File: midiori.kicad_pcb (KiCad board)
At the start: 2 copper layers, 141 x 150 mm, 45 parts, among them J1 x68000_expansion, J2 Conn_ARM_JTAG_SWD_10, J4 Mini-DIN-5, U1 74LCX07, U10 ICE40HX1K-VQ100, U11 TLV73333PDBV, U2 AT25SF081-SSHD-X, U3 TLV73312PDBV, U4 SN74LVC8T245DWR, U5 SN74LVC8T245DWR, U6 SN74LVC8T245DWR, U7 SN74LVC8T245DWR, U8 SN74LVC8T245DWR, U9 SN74LVC8T245DWR, X1 16MHz

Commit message: convert pcb version
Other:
- net class Default removed

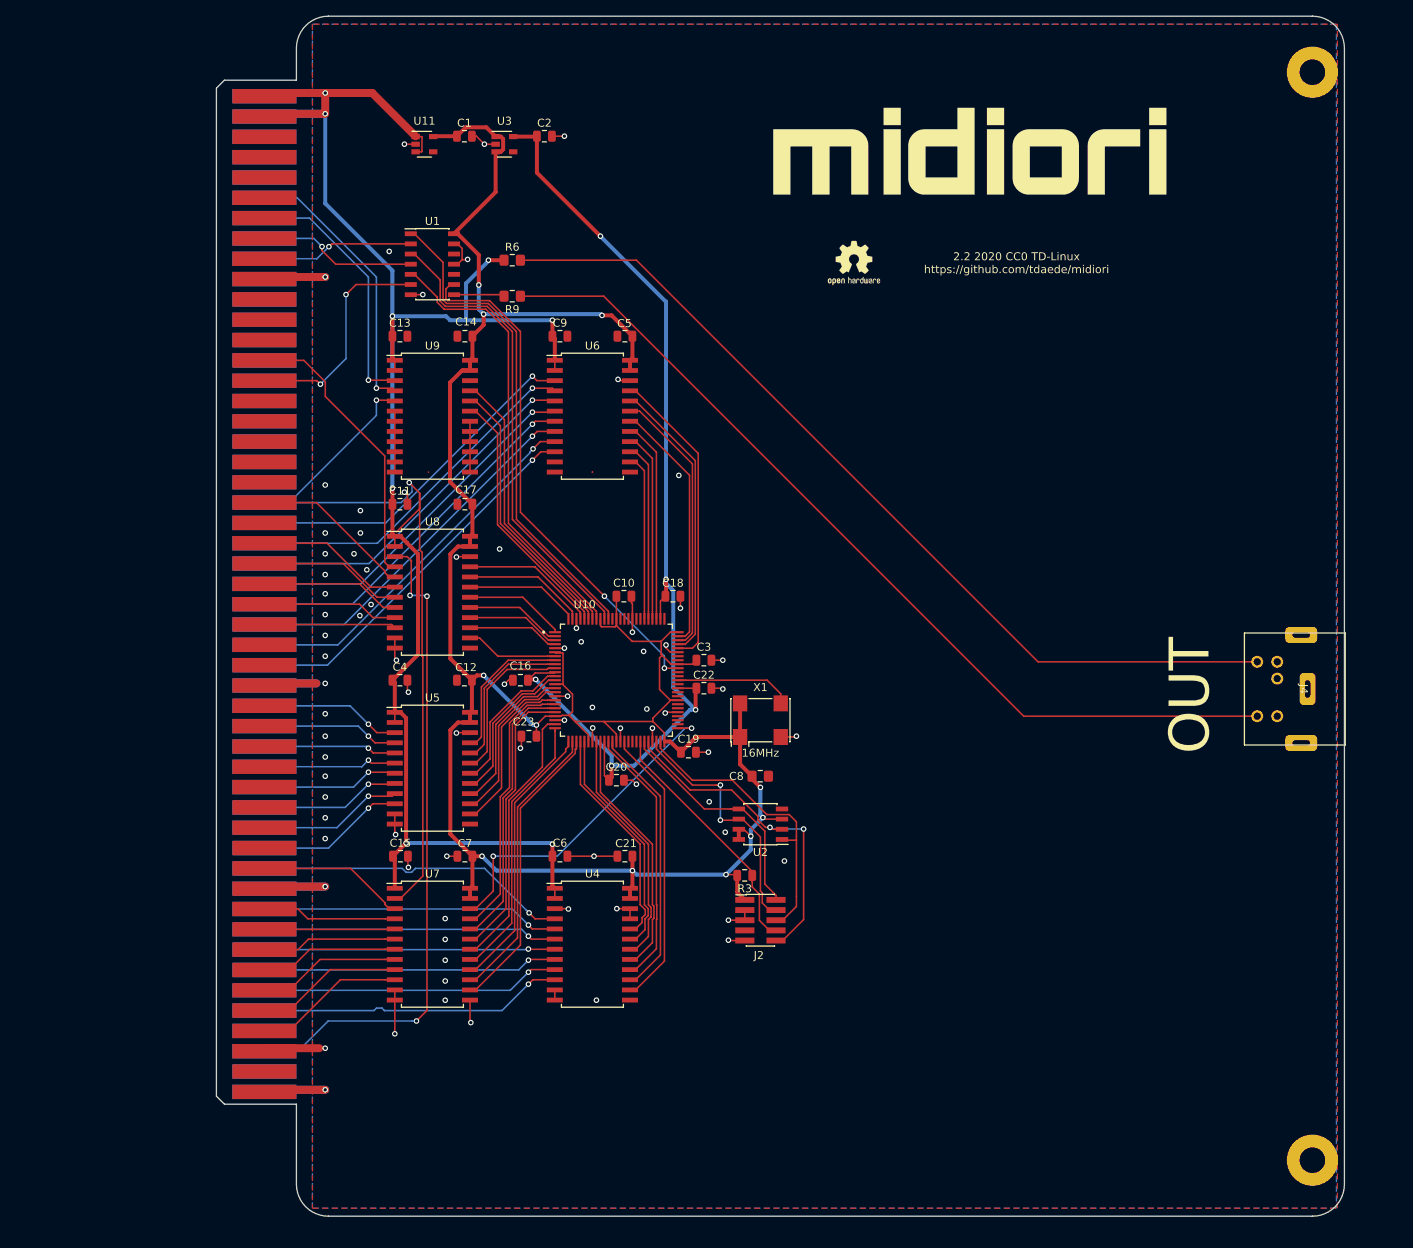
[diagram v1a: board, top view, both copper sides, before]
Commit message: switch to single psu translator
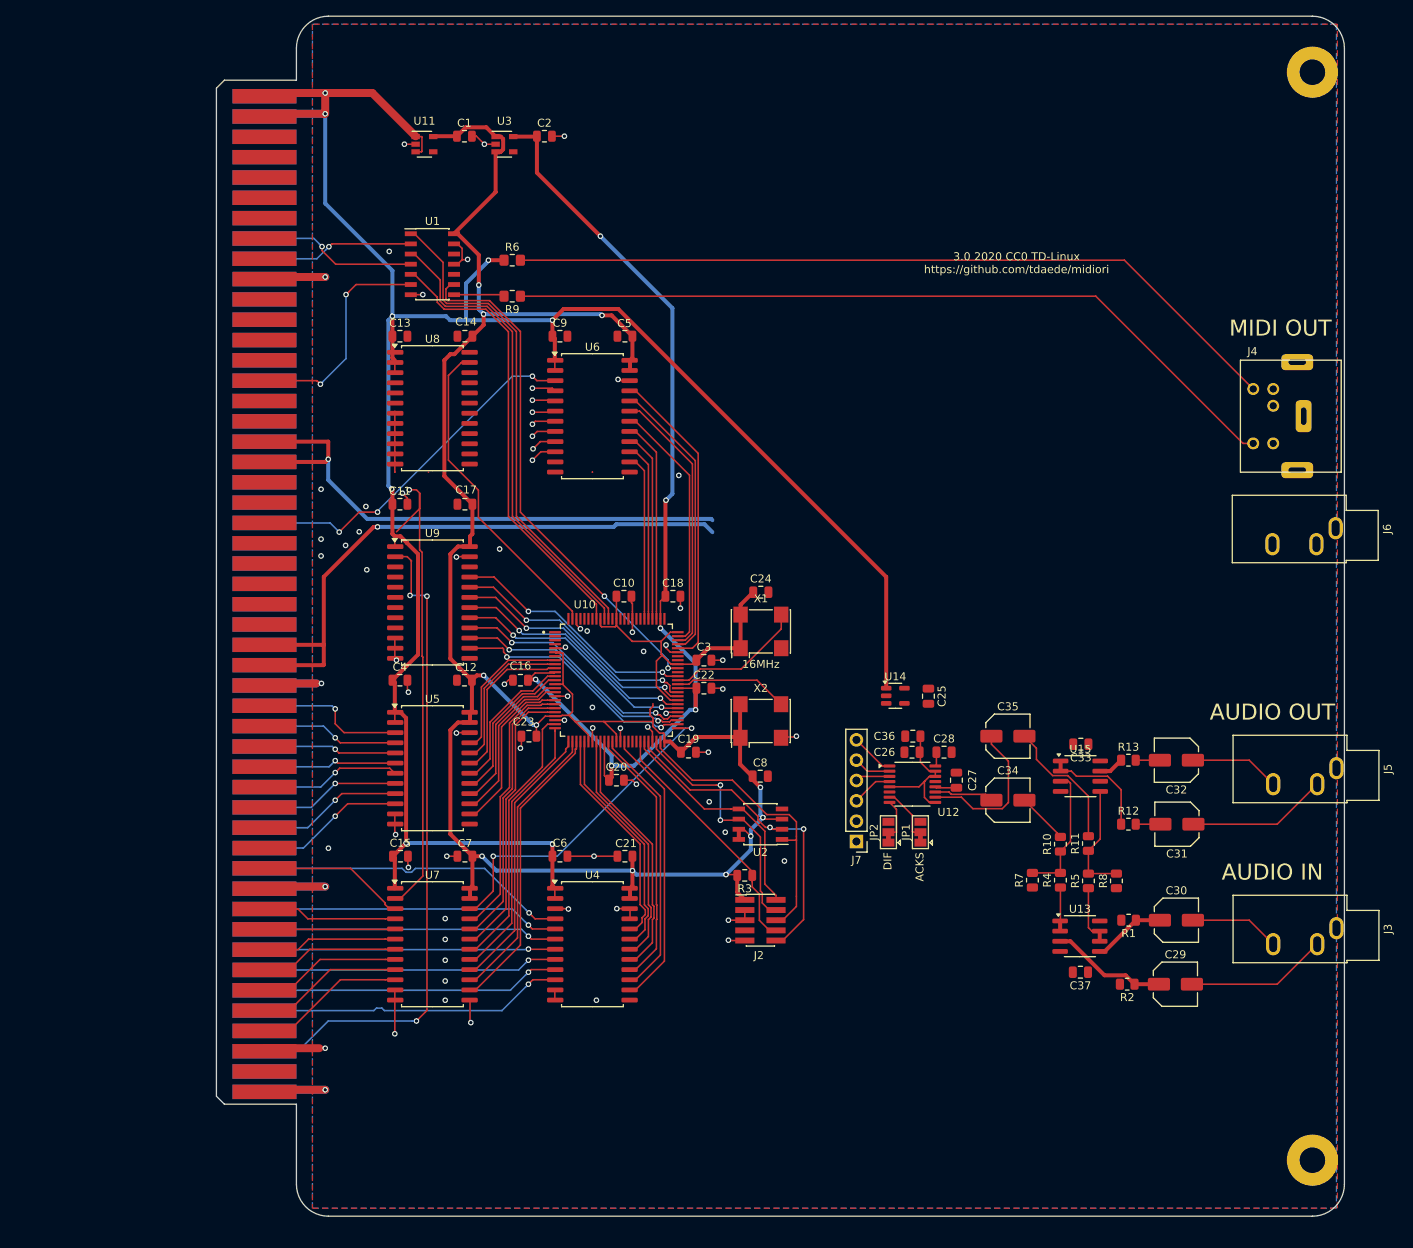
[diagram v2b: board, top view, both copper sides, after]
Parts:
- removed REF**: OSHW-Logo2_7.3x6mm_SilkScreen, Symbol:OSHW-Logo2_7.3x6mm_SilkScreen
- removed svg2mod: G***, x68k:midiori_logo
- added C24: 0.1uF, Capacitor_SMD:C_0805_2012Metric, F.Cu at (112.0, 111.0)
- added C25: 4.7uF, Capacitor_SMD:C_0805_2012Metric, F.Cu at (133.0, 124.0)
- added C26: 0.1uF, Capacitor_SMD:C_0805_2012Metric, F.Cu at (130.9, 131.0)
- added C27: 2.2uF, Capacitor_SMD:C_0805_2012Metric, F.Cu at (136.5, 134.5)
- added C28: 1uF, Capacitor_SMD:C_0805_2012Metric, F.Cu at (134.9, 131.0)
- added C29: 10uF, Capacitor_SMD:C_Elec_5x5.8, F.Cu at (163.9, 160.0)
- added C30: 10uF, Capacitor_SMD:C_Elec_5x5.8, F.Cu at (164.0, 152.0)
- added C31: 10uF, Capacitor_SMD:C_Elec_5x5.8, F.Cu at (164.1, 140.0)
- added C32: 10uF, Capacitor_SMD:C_Elec_5x5.8, F.Cu at (164.0, 132.0)
- added C33: 0.1uF, Capacitor_SMD:C_0805_2012Metric, F.Cu at (152.1, 130.0)
- added C34: 10uF, Capacitor_SMD:C_Elec_5x5.8, F.Cu at (142.9, 137.0)
- added C35: 10uF, Capacitor_SMD:C_Elec_5x5.8, F.Cu at (142.9, 129.0)
- added C36: 4.7uF, Capacitor_SMD:C_0805_2012Metric, F.Cu at (131.1, 129.0)
- added C37: 0.1uF, Capacitor_SMD:C_0805_2012Metric, F.Cu at (152.0, 158.5)
- added J3: AudioJack3, Connector_Audio:Jack_3.5mm_CUI_SJ1-3533NG_Horizontal, F.Cu at (184.0, 153.0)
- added J5: AudioJack3, Connector_Audio:Jack_3.5mm_CUI_SJ1-3533NG_Horizontal, F.Cu at (184.0, 133.0)
- added J6: AudioJack3, Connector_Audio:Jack_3.5mm_CUI_SJ1-3533NG_Horizontal, F.Cu at (183.9, 103.0)
- added J7: Conn_01x06, Connector_PinHeader_2.54mm:PinHeader_1x06_P2.54mm_Vertical, F.Cu at (124.0, 142.2)
- added JP1: ACKS, Jumper:SolderJumper-3_P1.3mm_Bridged12_Pad1.0x1.5mm, F.Cu at (132.0, 141.0)
- added JP2: DIF, Jumper:SolderJumper-3_P1.3mm_Bridged12_Pad1.0x1.5mm, F.Cu at (128.0, 141.0)
- added R1: 10k, Resistor_SMD:R_0805_2012Metric, F.Cu at (158.0, 152.0)
- added R10: 10k, Resistor_SMD:R_0805_2012Metric, F.Cu at (149.5, 142.5)
- added R11: 10k, Resistor_SMD:R_0805_2012Metric, F.Cu at (153.0, 142.4)
- added R12: 1k, Resistor_SMD:R_0805_2012Metric, F.Cu at (158.0, 140.0)
- added R13: 1k, Resistor_SMD:R_0805_2012Metric, F.Cu at (158.0, 132.0)
- added R2: 10k, Resistor_SMD:R_0805_2012Metric, F.Cu at (157.8, 160.0)
- added R4: 10k, Resistor_SMD:R_0805_2012Metric, F.Cu at (149.5, 147.0)
- added R5: 10k, Resistor_SMD:R_0805_2012Metric, F.Cu at (153.0, 147.1)
- added R7: 10k, Resistor_SMD:R_0805_2012Metric, F.Cu at (146.0, 147.0)
- added R8: 10k, Resistor_SMD:R_0805_2012Metric, F.Cu at (156.5, 147.1)
- added U12: AK4432, Package_SO:TSSOP-16_4.4x5mm_P0.65mm, F.Cu at (131.0, 135.0)
- added U13: TL074, Package_SO:SOIC-8_3.9x4.9mm_P1.27mm, F.Cu at (151.9, 154.0)
- added U14: AP2205K-3.3, Package_TO_SOT_SMD:SOT-23-5, F.Cu at (128.9, 124.0)
- added U15: TL072, Package_SO:SOIC-8_3.9x4.9mm_P1.27mm, F.Cu at (152.0, 134.0)
- added X2: 24.576MHz, Oscillator:Oscillator_SMD_SeikoEpson_SG8002CA-4Pin_7.0x5.0mm, F.Cu at (112.0, 127.1)
- C8: footprint Capacitor_SMD:C_0805_2012Metric_Pad1.15x1.40mm_HandSolder -> Capacitor_SMD:C_0805_2012Metric
- J1: value x68000_expansion -> midiori-rescue_x68000_expansion-x68k-midiori-rescue
- U11: value TLV73333PDBV -> AP2205K-3.3
- U3: value TLV73312PDBV -> AP2127K-1.2
- moved J4 34.1 mm to (179.9, 89.0)
- moved U9 23.3 mm to (71.0, 112.3)
- moved U8 23.0 mm to (71.0, 88.0)
- moved X1 11.1 mm to (112.1, 115.9)
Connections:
- net Net-(J4-Pad4) renamed /source
- net Net-(J4-Pad5) renamed /sink
- net Net-(U10-Pad63) renamed /16mhz
- J1 pad A13: Net-(J1-PadA13) -> /DB8
- J1 pad A14: Net-(J1-PadA14) -> /DB9
- J1 pad A15: Net-(J1-PadA15) -> /DB10
- J1 pad A16: Net-(J1-PadA16) -> /DB11
- J1 pad A17: Net-(J1-PadA17) -> /DB12
- J1 pad A18: Net-(J1-PadA18) -> /DB13
- J1 pad A19: Net-(J1-PadA19) -> /DB14
- J1 pad A2: Net-(J1-PadA2) -> unconnected-(J1-PadA2)
- J1 pad A20: Net-(J1-PadA20) -> /DB15
- J1 pad A22: Net-(J1-PadA22) -> +12V
- J1 pad A23: Net-(J1-PadA23) -> +12V
- J1 pad A24: /C -> unconnected-(J1-FC0-PadA24)
- J1 pad A25: /B -> unconnected-(J1-FC1-PadA25)
- J1 pad A26: /A -> unconnected-(J1-FC2-PadA26)
- J1 pad A29: Net-(J1-PadA29) -> unconnected-(J1-PadA29)
- J1 pad A31: Net-(J1-PadA31) -> unconnected-(J1-PadA31)
- J1 pad A32: Net-(J1-PadA32) -> -12V
- J1 pad A33: Net-(J1-PadA33) -> -12V
- J1 pad A34: Net-(J1-PadA34) -> unconnected-(J1-PadA34)
- J1 pad A35: Net-(J1-PadA35) -> unconnected-(J1-PadA35)
- J1 pad A38: Net-(J1-PadA38) -> unconnected-(J1-PadA38)
- J1 pad A39: Net-(J1-PadA39) -> unconnected-(J1-PadA39)
- J1 pad A40: Net-(J1-PadA40) -> unconnected-(J1-PadA40)
- J1 pad A42: Net-(J1-PadA42) -> unconnected-(J1-PadA42)
- J1 pad A43: Net-(J1-PadA43) -> unconnected-(J1-PadA43)
- J1 pad A44: Net-(J1-PadA44) -> unconnected-(J1-PadA44)
- J1 pad A45: Net-(J1-PadA45) -> unconnected-(J1-PadA45)
- J1 pad A46: Net-(J1-PadA46) -> unconnected-(J1-PadA46)
- J1 pad A47: Net-(J1-PadA47) -> unconnected-(J1-PadA47)
- J1 pad A48: Net-(J1-PadA48) -> unconnected-(J1-PadA48)
- J1 pad B2: Net-(J1-PadB2) -> unconnected-(J1-PadB2)
- J1 pad B31: Net-(J1-PadB31) -> unconnected-(J1-PadB31)
- J1 pad B32: Net-(J1-PadB32) -> unconnected-(J1-PadB32)
- J1 pad B33: Net-(J1-PadB33) -> unconnected-(J1-PadB33)
- J1 pad B34: Net-(J1-PadB34) -> unconnected-(J1-PadB34)
- J1 pad B35: Net-(J1-PadB35) -> unconnected-(J1-PadB35)
- J1 pad B36: Net-(J1-PadB36) -> unconnected-(J1-PadB36)
- J1 pad B37: Net-(J1-PadB37) -> unconnected-(J1-PadB37)
- J1 pad B38: Net-(J1-PadB38) -> unconnected-(J1-PadB38)
- J1 pad B39: Net-(J1-PadB39) -> unconnected-(J1-PadB39)
- J1 pad B4: Net-(J1-PadB4) -> unconnected-(J1-PadB4)
- J1 pad B40: Net-(J1-PadB40) -> unconnected-(J1-PadB40)
- J1 pad B46: Net-(J1-PadB46) -> unconnected-(J1-PadB46)
- J1 pad B47: Net-(J1-PadB47) -> unconnected-(J1-PadB47)
- J1 pad B48: Net-(J1-PadB48) -> unconnected-(J1-PadB48)
- J2 pad 7: Net-(J2-Pad7) -> unconnected-(J2-KEY-Pad7)
- J4 pad 1: Net-(J4-Pad1) -> unconnected-(J4-Pad1)
- J4 pad 3: Net-(J4-Pad3) -> unconnected-(J4-Pad3)
- U1 pad 10: Net-(U1-Pad10) -> unconnected-(U1-Pad10)
- U1 pad 12: Net-(U1-Pad12) -> unconnected-(U1-Pad12)
- U10 pad 3: /a -> unconnected-(U10-IOL_2A-Pad3)
- U10 pad 4: /b -> unconnected-(U10-IOL_2B-Pad4)
- U10 pad 41: Net-(U10-Pad41) -> unconnected-(U10-IOB_42_CBSEL0-Pad41)
- U10 pad 42: Net-(U10-Pad42) -> unconnected-(U10-IOB_43_CBSEL1-Pad42)
- U10 pad 43: Net-(U10-Pad43) -> unconnected-(U10-CDONE-Pad43)
- U10 pad 52: Net-(U10-Pad52) -> /db8
- U10 pad 53: Net-(U10-Pad53) -> /db9
- U10 pad 54: Net-(U10-Pad54) -> /db10
- U10 pad 56: Net-(U10-Pad56) -> /db11
- U10 pad 57: Net-(U10-Pad57) -> /db12
- U10 pad 59: Net-(U10-Pad59) -> /db13
- U10 pad 60: Net-(U10-Pad60) -> /db14
- U10 pad 62: Net-(U10-Pad62) -> /24.576mhz
- U10 pad 64: Net-(U10-Pad64) -> /db15
- U10 pad 65: Net-(U10-Pad65) -> unconnected-(U10-IOR_64-Pad65)
- U10 pad 68: Net-(U10-Pad68) -> unconnected-(U10-IOR_67-Pad68)
- U10 pad 69: Net-(U10-Pad69) -> unconnected-(U10-IOR_68-Pad69)
- U10 pad 7: /c -> unconnected-(U10-IOL_3A-Pad7)
- U10 pad 76: Net-(U10-Pad76) -> unconnected-(U10-VPP_FAST-Pad76)
- U10 pad 82: Net-(U10-Pad82) -> unconnected-(U10-IOT_78-Pad82)
- U10 pad 83: Net-(U10-Pad83) -> unconnected-(U10-IOT_79-Pad83)
- U10 pad 85: Net-(U10-Pad85) -> /smute
- U10 pad 86: Net-(U10-Pad86) -> /sdti
- U10 pad 87: Net-(U10-Pad87) -> /lrck
- U10 pad 89: Net-(U10-Pad89) -> /bick
- U11 pad 4: Net-(U11-Pad4) -> unconnected-(U11-NC-Pad4)
- U3 pad 1: +3V3 -> +5V
- U3 pad 3: +3V3 -> +5V
- U3 pad 4: Net-(U3-Pad4) -> unconnected-(U3-NC-Pad4)
- U8 pad 10: /C -> /IDDIR
- U8 pad 14: /c -> /iddir
- U8 pad 15: /b -> /iack4
- U8 pad 16: /a -> /iack2
- U8 pad 8: /A -> /IACK2
- U8 pad 9: /B -> /IACK4
- U9 pad 10: GND -> /DB8
- U9 pad 14: GND -> /db8
- U9 pad 15: GND -> /db9
- U9 pad 16: GND -> /db10
- U9 pad 17: GND -> /db11
- U9 pad 18: GND -> /db12
- U9 pad 19: /iddir -> /db13
- U9 pad 2: +5V -> /IDDIR
- U9 pad 20: /iack4 -> /db14
- U9 pad 21: /iack2 -> /db15
- U9 pad 22: GND -> /xltr_oe
- U9 pad 3: /IACK2 -> /DB15
- U9 pad 4: /IACK4 -> /DB14
- U9 pad 5: /IDDIR -> /DB13
- U9 pad 6: GND -> /DB12
- U9 pad 7: GND -> /DB11
- U9 pad 8: GND -> /DB10
- U9 pad 9: GND -> /DB9
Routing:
- net +12V: track 0.00 -> 77.6 mm, vias 0 -> 1
- net -12V: track 0.00 -> 71.0 mm, vias 0 -> 2
- net +5V: track 227.3 -> 297.8 mm
- net /AB16: track 47.3 -> 3.24 mm
- net /AB17: track 46.9 -> 3.09 mm
- net /IDDIR: track 103.6 -> 60.1 mm, vias 2 -> 1
- net /AB18: track 49.4 -> 6.15 mm
- net /AB19: track 45.8 -> 2.95 mm
- net /AB20: track 45.2 -> 2.86 mm
- net /AB21: track 44.8 -> 2.84 mm
- net /AB22: track 44.5 -> 2.93 mm
- net /EXRESET: track 35.9 -> 0.00 mm
- net /iack2: track 35.3 -> 0.00 mm
- net /IACK4: track 34.4 -> 0.00 mm, vias 1 -> 0
- net /iack4: track 33.8 -> 0.00 mm
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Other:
- board text added: "3.0 2020 CC0 TD-Linux https://github.com/tdaede/midiori"
- board text added: "ACKS"
- board text added: "AUDIO IN"
- board text added: "AUDIO OUT"
- board text added: "DIF"
- board text added: "MIDI OUT"
- board text removed: "2.2 2020 CC0 TD-Linux https://github.com/tdaede/midiori"
- board text removed: "OUT"

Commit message: aaaaaaaaaaa
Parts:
- removed C11, C13, C15, C4, C6, C9: 0.1uF, Capacitor_SMD:C_0805_2012Metric
- added J8: AudioJack3, Connector_Audio:Jack_3.5mm_CUI_SJ1-3533NG_Horizontal, F.Cu at (183.8, 114.9)
- added J9: Mini-DIN-5, x68k:MD-50SM, F.Cu at (179.9, 101.0)
- added JP3: Jumper_3_Bridged12, Jumper:SolderJumper-3_P1.3mm_Bridged12_Pad1.0x1.5mm, F.Cu at (21.1, 57.4)
- added JP4: Jumper_3_Bridged12, Jumper:SolderJumper-3_P1.3mm_Bridged12_Pad1.0x1.5mm, F.Cu at (21.1, 61.2)
- added JP5: Jumper_3_Bridged12, Jumper:SolderJumper-3_P1.3mm_Bridged12_Pad1.0x1.5mm, F.Cu at (21.1, 65.1)
- added R14: 10k, Resistor_SMD:R_0805_2012Metric, F.Cu at (26.1, 57.1)
- added R15: 220, Resistor_SMD:R_0805_2012Metric, F.Cu at (26.1, 60.0)
- added R16: 220, Resistor_SMD:R_0805_2012Metric, F.Cu at (26.1, 63.0)
- added U16: 74LCX07, Package_SO:SOIC-14_3.9x8.7mm_P1.27mm, F.Cu at (90.0, 80.5)
- added U17: PC817, Package_DIP:DIP-4_W7.62mm, F.Cu at (152.2, 110.7)
- added U18: SN74LVC245APW, Package_SO:SOIC-20W_7.5x12.8mm_P1.27mm, F.Cu at (71.0, 64.0)
- R6, R9: footprint Resistor_SMD:R_0805_2012Metric_Pad1.15x1.40mm_HandSolder -> Resistor_SMD:R_0805_2012Metric
- U4, U5, U6, U7, U8, U9: value SN74LVC8T245DWR -> SN74LVC245APW; footprint Package_SO:SOIC-24W_7.5x15.4mm_P1.27mm -> Package_SO:SOIC-20W_7.5x12.8mm_P1.27mm
- moved C2 56.1 mm to (114.0, 102.1), turned to -90 degrees
- moved U3 55.9 mm to (110.1, 102.0)
- moved R9 33.1 mm to (114.0, 77.0)
- moved R6 26.0 mm to (107.0, 69.0)
- moved U6 22.8 mm to (71.0, 100.0)
- moved U1 20.4 mm to (90.0, 62.5)
- moved J6 20.1 mm to (183.8, 82.9)
- moved J4 20.0 mm to (179.9, 69.0)
- moved U8 6.00 mm to (71.0, 82.0)
- moved U9 5.72 mm to (71.0, 118.0)
- moved U11 4.03 mm to (70.5, 51.0)
- moved U5 3.00 mm to (71.0, 136.0)
- moved C1 2.98 mm to (74.5, 51.1), turned to -90 degrees
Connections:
- net Net-(U10-IOR_65) renamed /midi_out
- J1 pad B36: unconnected-(J1-PadB36) -> /EXREQ
- J1 pad B37: unconnected-(J1-PadB37) -> /EXACK
- J1 pad B39: unconnected-(J1-PadB39) -> /EXOWN
- J1 pad B46: unconnected-(J1-PadB46) -> /BR
- J1 pad B47: unconnected-(J1-PadB47) -> /BG
- J1 pad B48: unconnected-(J1-PadB48) -> /BGACK
- U1 pad 10: unconnected-(U1-Pad10) -> /BR
- U1 pad 11: GND -> /br
- U1 pad 12: unconnected-(U1-Pad12) -> /UDS
- U1 pad 13: GND -> /uds_lds_drv
- U1 pad 5: /dtack -> /dtack_drv
- U10 pad 3: unconnected-(U10-IOL_2A-Pad3) -> /bg
- U10 pad 4: unconnected-(U10-IOL_2B-Pad4) -> /midi_in
- U10 pad 41: unconnected-(U10-IOB_42_CBSEL0-Pad41) -> /rw_drv
- U10 pad 42: unconnected-(U10-IOB_43_CBSEL1-Pad42) -> /as_drv
- U10 pad 65: unconnected-(U10-IOR_64-Pad65) -> /bgack
- U10 pad 68: unconnected-(U10-IOR_67-Pad68) -> /br
- U10 pad 69: unconnected-(U10-IOR_68-Pad69) -> /data_dir
- U10 pad 7: unconnected-(U10-IOL_3A-Pad7) -> /uds_lds_drv
- U10 pad 82: unconnected-(U10-IOT_78-Pad82) -> /dtack
- U10 pad 83: unconnected-(U10-IOT_79-Pad83) -> Net-(JP4-C)
- U10 pad 89: /bick -> /10m
- U10 pad 93: /dtack -> /dtack_drv
- U10 pad 97: /10m -> /exown
- U4 pad 1: +5V -> /addr_dir
- U4 pad 10: /AB1 -> GND
- U4 pad 11: GND -> /a1
- U4 pad 12: GND -> /a2
- U4 pad 13: GND -> /a3
- U4 pad 14: /a1 -> /a4
- U4 pad 15: /a2 -> /a5
- U4 pad 16: /a3 -> /a6
- U4 pad 17: /a4 -> /a7
- U4 pad 18: /a5 -> GND
- U4 pad 19: /a6 -> GND
- U4 pad 2: +5V -> GND
- U4 pad 20: /a7 -> +3V3
- U4 pad 3: GND -> /AB7
- U4 pad 4: /AB7 -> /AB6
- U4 pad 5: /AB6 -> /AB5
- U4 pad 6: /AB5 -> /AB4
- U4 pad 7: /AB4 -> /AB3
- U4 pad 8: /AB3 -> /AB2
- U4 pad 9: /AB2 -> /AB1
- U5 pad 1: +5V -> /addr_dir
- U5 pad 10: /AB8 -> GND
- U5 pad 11: GND -> /ab8
- U5 pad 12: GND -> /ab9
- U5 pad 13: GND -> /ab10
- U5 pad 14: /ab8 -> /ab11
- U5 pad 15: /ab9 -> /ab12
- U5 pad 16: /ab10 -> /ab13
- U5 pad 17: /ab11 -> /ab14
- U5 pad 18: /ab12 -> /ab15
- U5 pad 19: /ab13 -> GND
- U5 pad 2: +5V -> /AB15
- U5 pad 20: /ab14 -> +3V3
- U5 pad 3: /AB15 -> /AB14
- U5 pad 4: /AB14 -> /AB13
- U5 pad 5: /AB13 -> /AB12
- U5 pad 6: /AB12 -> /AB11
- U5 pad 7: /AB11 -> /AB10
- U5 pad 8: /AB10 -> /AB9
- U5 pad 9: /AB9 -> /AB8
- U6 pad 1: +5V -> /addr_dir
- U6 pad 10: /AB16 -> GND
- U6 pad 11: GND -> /a16
- U6 pad 12: GND -> /a17
- U6 pad 13: GND -> /a18
- U6 pad 14: /a16 -> /a19
- U6 pad 15: /a17 -> /a20
- U6 pad 16: /a18 -> /a21
- U6 pad 17: /a19 -> /a22
- U6 pad 18: /a20 -> /a23
- U6 pad 19: /a21 -> GND
- U6 pad 2: +5V -> /AB23
- U6 pad 20: /a22 -> +3V3
- U6 pad 3: /AB23 -> /AB22
- U6 pad 4: /AB22 -> /AB21
- U6 pad 5: /AB21 -> /AB20
- U6 pad 6: /AB20 -> /AB19
- U6 pad 7: /AB19 -> /AB18
- U6 pad 8: /AB18 -> /AB17
- U6 pad 9: /AB17 -> /AB16
- U7 pad 1: +5V -> /data_dir
- U7 pad 10: /DB0 -> GND
- U7 pad 11: GND -> /d0
- U7 pad 12: GND -> /d1
- U7 pad 13: GND -> /d2
- U7 pad 14: /d0 -> /d3
- U7 pad 15: /d1 -> /d4
- U7 pad 16: /d2 -> /d5
- U7 pad 17: /d3 -> /d6
- U7 pad 18: /d4 -> /d7
- U7 pad 19: /d5 -> /xltr_oe
- U7 pad 2: /IDDIR -> /DB7
- U7 pad 20: /d6 -> +3V3
- U7 pad 3: /DB7 -> /DB6
- U7 pad 4: /DB6 -> /DB5
- U7 pad 5: /DB5 -> /DB4
- U7 pad 6: /DB4 -> /DB3
- U7 pad 7: /DB3 -> /DB2
- U7 pad 8: /DB2 -> /DB1
- U7 pad 9: /DB1 -> /DB0
- U8 pad 1: +5V -> +3V3
- U8 pad 10: /IDDIR -> GND
- U8 pad 11: GND -> /iddir
- U8 pad 12: GND -> /iack4
- U8 pad 13: GND -> /iack2
- U8 pad 14: /iddir -> /as
- U8 pad 15: /iack4 -> /lds
- U8 pad 16: /iack2 -> /rw
- U8 pad 17: /as -> /exreset
- U8 pad 18: /lds -> /10m
- U8 pad 19: /rw -> GND
- U8 pad 2: +5V -> /10MHz
- U8 pad 20: /exreset -> +3V3
- U8 pad 3: /10MHz -> /EXRESET
- U8 pad 4: /EXRESET -> /RW
- U8 pad 5: /RW -> /LDS
- U8 pad 6: /LDS -> /AS
- U8 pad 7: /AS -> /IACK2
- U8 pad 8: /IACK2 -> /IACK4
- U8 pad 9: /IACK4 -> /IDDIR
- U9 pad 1: +5V -> /data_dir
- U9 pad 10: /DB8 -> GND
- U9 pad 11: GND -> /db8
- U9 pad 12: GND -> /db9
- U9 pad 13: GND -> /db10
- U9 pad 14: /db8 -> /db11
- U9 pad 15: /db9 -> /db12
- U9 pad 16: /db10 -> /db13
- U9 pad 17: /db11 -> /db14
- U9 pad 18: /db12 -> /db15
- U9 pad 19: /db13 -> /xltr_oe
- U9 pad 2: /IDDIR -> /DB15
- U9 pad 20: /db14 -> +3V3
- U9 pad 3: /DB15 -> /DB14
- U9 pad 4: /DB14 -> /DB13
- U9 pad 5: /DB13 -> /DB12
- U9 pad 6: /DB12 -> /DB11
- U9 pad 7: /DB11 -> /DB10
- U9 pad 8: /DB10 -> /DB9
- U9 pad 9: /DB9 -> /DB8
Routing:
- net +3V3: track 323.9 -> 52.8 mm, vias 12 -> 1
- net +5V: track 297.8 -> 52.2 mm, vias 8 -> 2
- net /10MHz: track 83.1 -> 0.00 mm, vias 3 -> 0
- net /source: track 98.3 -> 22.8 mm
- net /sink: track 99.9 -> 28.0 mm
- net +1V2: track 129.2 -> 61.4 mm, vias 6 -> 4
- net +12V: track 77.6 -> 17.4 mm, vias 1 -> 0
- net /IDDIR: track 60.1 -> 0.00 mm, vias 1 -> 0
- net /dtack_drv: track 0.00 -> 56.0 mm
- net /dtack: track 56.0 -> 0.00 mm
- net -12V: track 71.0 -> 18.3 mm, vias 2 -> 1
- net /AB23: track 45.2 -> 0.00 mm, vias 3 -> 0
- net /IRQ4: track 19.9 -> 0.00 mm, vias 1 -> 0
- net /IRQ2: track 19.1 -> 0.00 mm
- net /AB15: track 18.8 -> 0.00 mm, vias 1 -> 0
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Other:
- board text added: "MIDI IN"
